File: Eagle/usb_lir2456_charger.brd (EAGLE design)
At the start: 36.8 x 47.5 mm, 15 parts

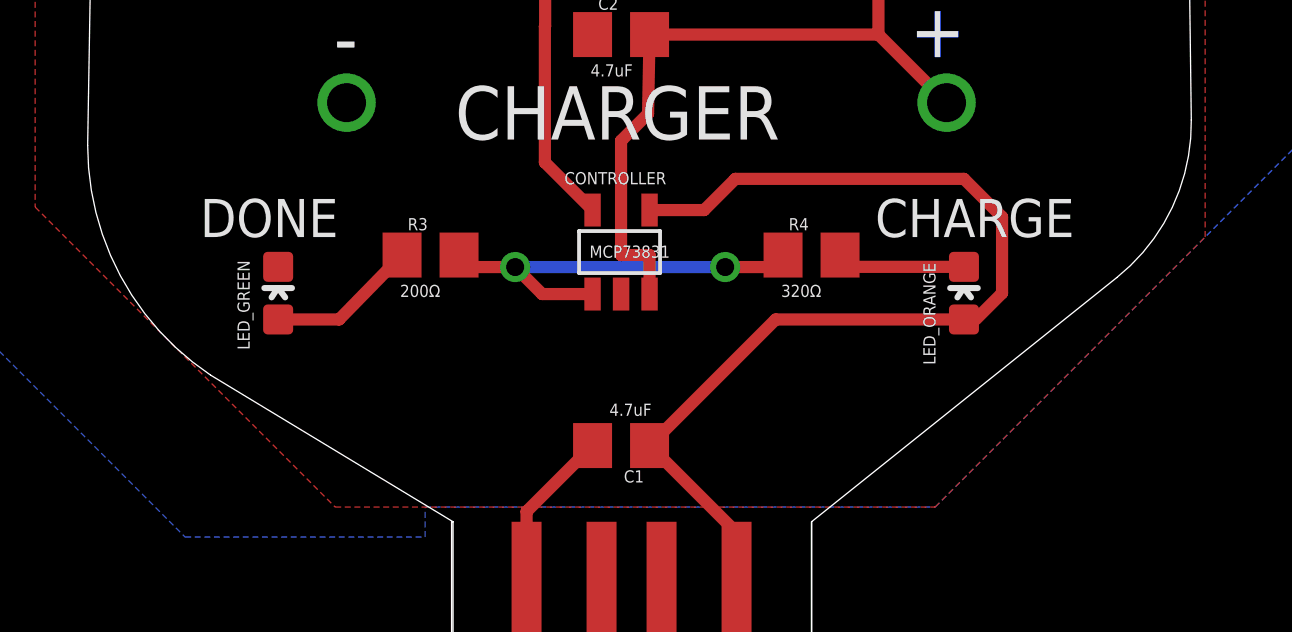
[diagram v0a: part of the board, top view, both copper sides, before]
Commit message: Edited Charge and Done Led connections
actually I have not able to test it is it correct or not. How ever next week i will be able to do it. Before it maybe some one could have chance before me. Best regards.  Note: I have get the idea from https://www.electroschematics.com/3-7v-li-ion-battery-charger-circuit/ that link.
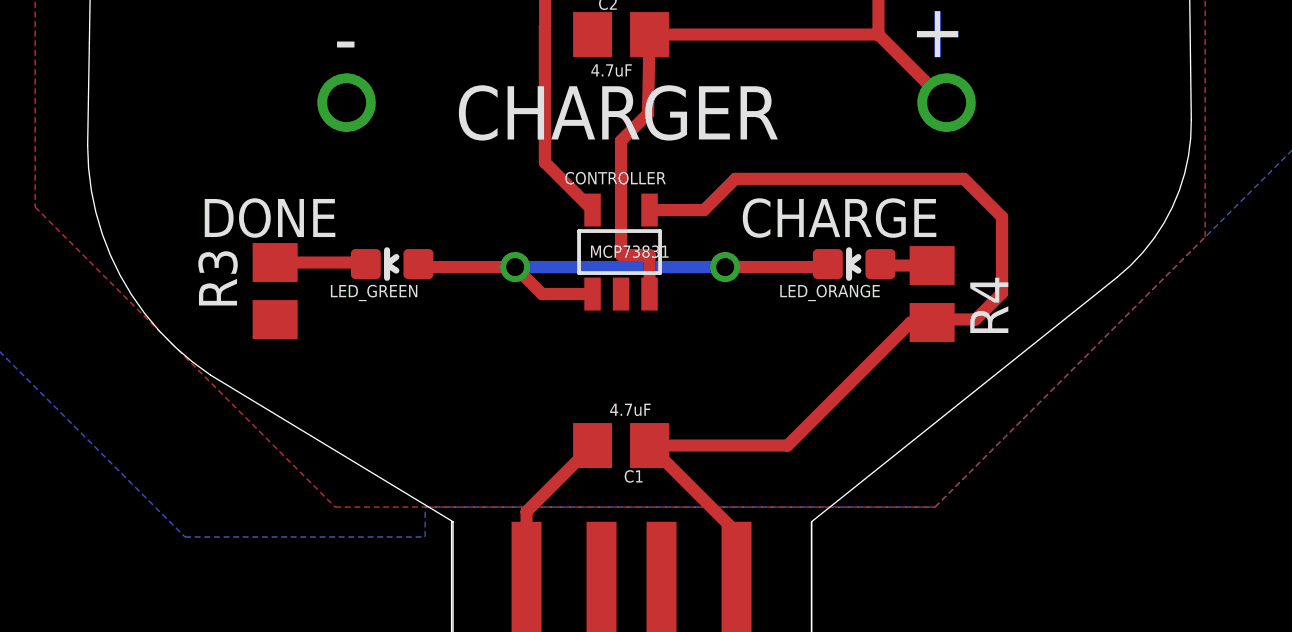
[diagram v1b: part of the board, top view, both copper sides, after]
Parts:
- R3: value 200Ω -> 470Ω
- R4: value 320Ω -> 470Ω
- moved R3 5.32 mm to (38.0, 24.2), turned to 90 degrees
- moved R4 4.22 mm to (59.9, 24.1), turned to 270 degrees
- moved LED_GREEN 3.92 mm to (41.9, 25.1), turned to 90 degrees
- moved LED_ORANGE 3.79 mm to (57.3, 25.1), turned to 90 degrees
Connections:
- net GND: now also R3.1; no longer LED_GREEN.C
- net N$1: now also LED_GREEN.A, LED_ORANGE.C; no longer R3.2, R4.1
- net N$4: now also LED_GREEN.C, R3.2; no longer LED_GREEN.A, R3.1
- net N$7: now also LED_ORANGE.A, R4.1; no longer LED_ORANGE.C, R4.2
- net VCC: now also R4.2; no longer LED_ORANGE.A
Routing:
- net N$1: track 14.0 -> 16.7 mm
- net N$7: track 4.31 -> 1.74 mm
- net N$4: track 5.03 -> 3.04 mm
